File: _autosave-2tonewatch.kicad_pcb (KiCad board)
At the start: 4 copper layers, 58 parts, among them IC1 MDBT50Q-P1MV2, J2 USB_C_Receptacle_USB2.0_16P, J3 Conn_01x02_Pin, J4 FFC-FPC_1X24_PIN, J5 Conn_01x04, Q1 Si1308EDL, SW1 SW_Push, SW2 SW_Push, SW3 SW_Push, SW4 SW_Push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

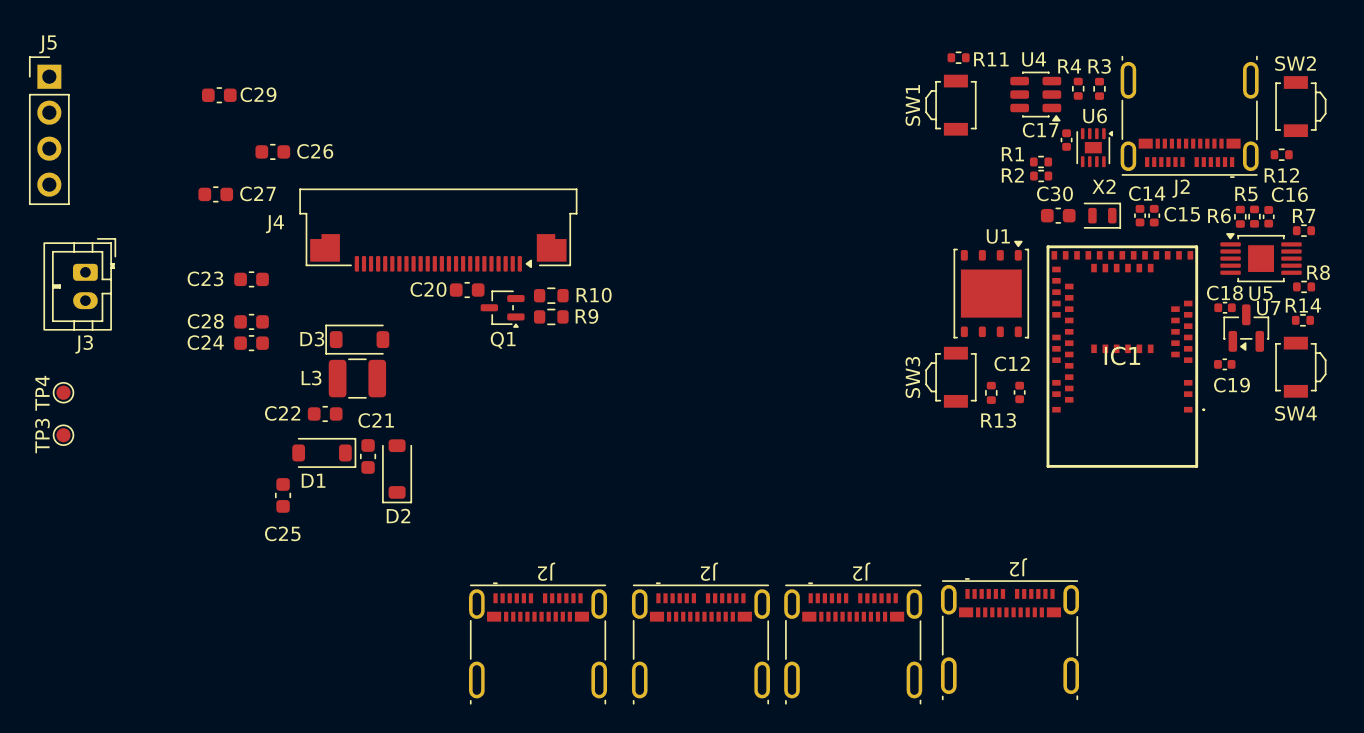
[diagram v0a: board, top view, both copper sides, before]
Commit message: Changed from stm32wb -> nRF52 module
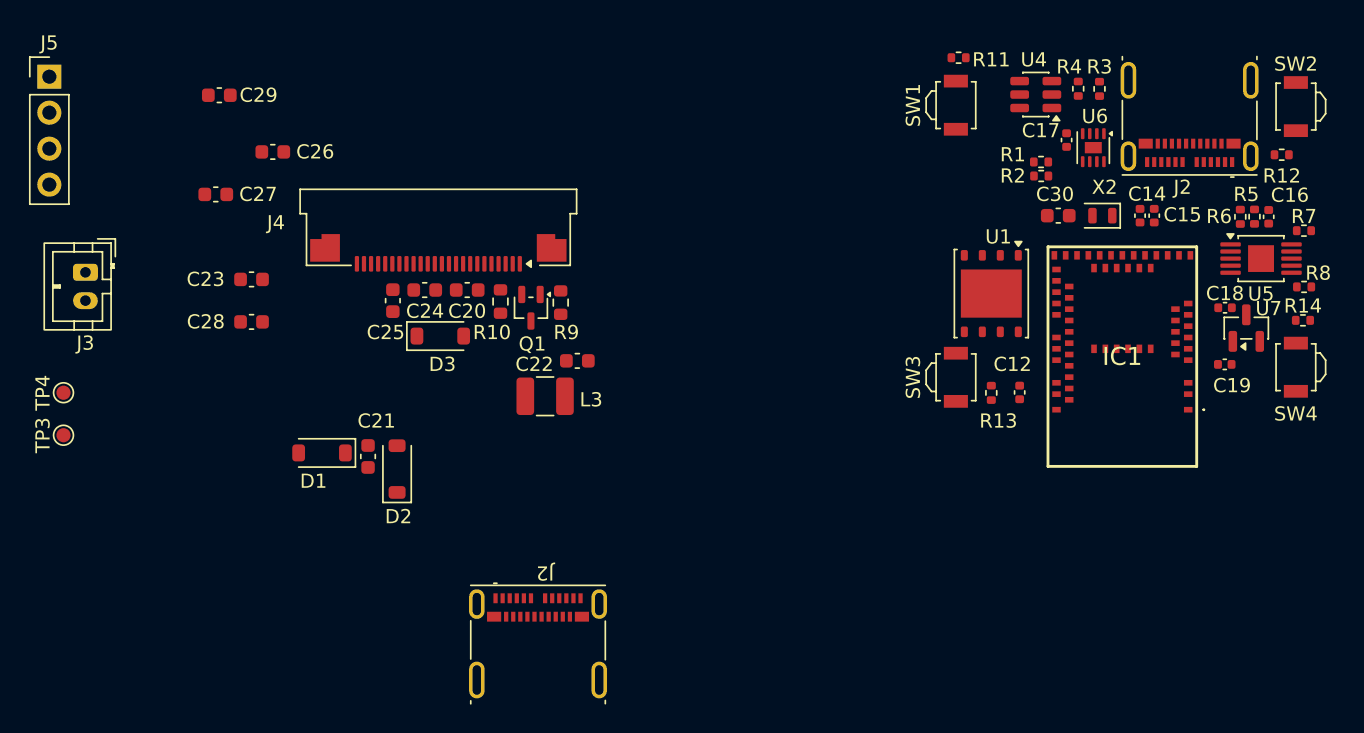
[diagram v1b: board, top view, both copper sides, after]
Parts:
- removed the J2 at (169.3, 128.4)
- removed the J2 at (147.5, 128.7)
- removed the J2 at (158.2, 128.7)
- moved C22 18.2 mm to (138.8, 108.8), turned to 0 degrees
- moved C25 15.8 mm to (125.8, 104.5)
- moved L3 13.3 mm to (136.5, 111.2), turned to 180 degrees
- moved C24 12.8 mm to (128.0, 103.8), turned to 0 degrees
- moved D3 5.71 mm to (129.1, 107.0)
- moved R10 3.61 mm to (133.3, 104.6), turned to -90 degrees
- moved Q1 2.00 mm to (135.5, 105.0), turned to -90 degrees
- moved R9 1.21 mm to (137.6, 104.6), turned to -90 degrees
